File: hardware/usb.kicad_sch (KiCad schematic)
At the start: 4 parts, among them J201 USB_C_Receptacle_USB2.0, U201 SRV05-4

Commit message: update to kicad 9
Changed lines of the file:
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@@
 (kicad_sch
-	(version 20231120)
+	(version 20250114)
 	(generator "eeschema")
-	(generator_version "8.0")
+	(generator_version "9.0")
 	(paper "A4")
 	(title_block
@@
 	(label "USB_5V"
 		(at 151.13 74.93 0)
-		(fields_autoplaced yes)
 		(effects
 			(font
@@
 		(shape bidirectional)
 		(at 199.39 88.9 0)
-		(fields_autoplaced yes)
 		(effects
 			(font
@@
 		(shape bidirectional)
 		(at 135.89 86.36 0)
-		(fields_autoplaced yes)
 		(effects
 			(font
@@
 		(shape bidirectional)
 		(at 135.89 82.55 0)
-		(fields_autoplaced yes)
 		(effects
 			(font
@@
 		(shape bidirectional)
 		(at 135.89 96.52 0)
-		(fields_autoplaced yes)
 		(effects
 			(font
@@
 		(shape bidirectional)
 		(at 199.39 93.98 0)
-		(fields_autoplaced yes)
 		(effects
 			(font
@@
 		(shape bidirectional)
 		(at 135.89 80.01 0)
-		(fields_autoplaced yes)
-		(effects
-			(font
+		(effects
+			(font

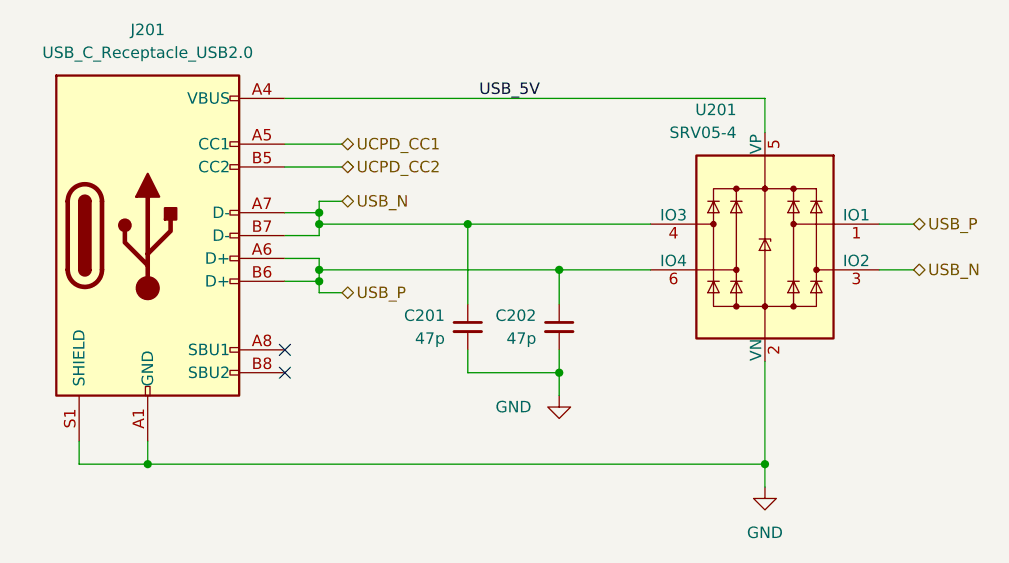
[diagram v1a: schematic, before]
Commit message: fix BOM to use basic parts again
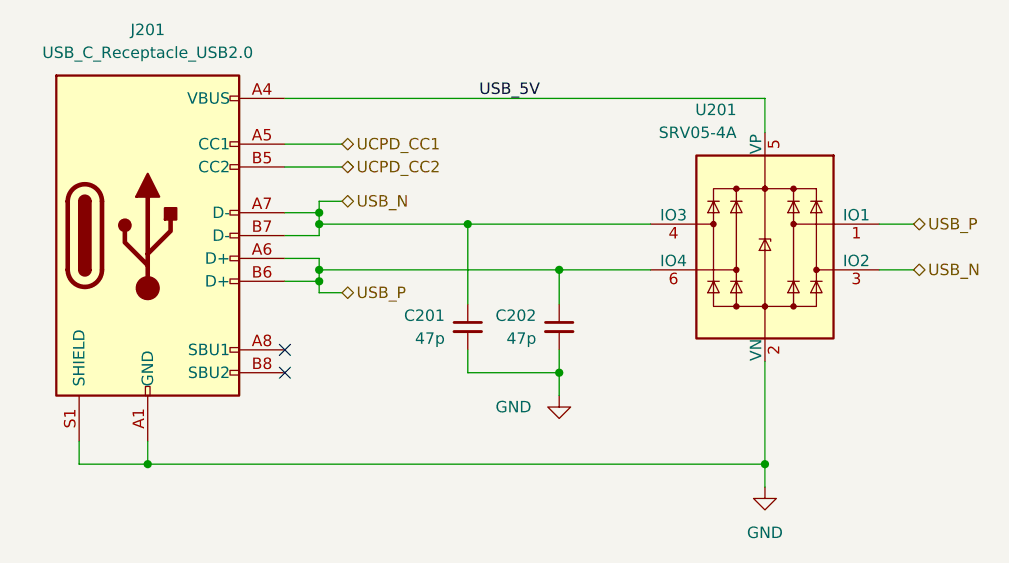
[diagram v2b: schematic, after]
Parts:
- U201: value SRV05-4 -> SRV05-4A; LCSC ID C7420376 -> C20615829
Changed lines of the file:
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@@
 			)
 		)
-		(property "Value" "SRV05-4"
+		(property "Value" "SRV05-4A"
 			(at 179.7303 78.74 0)
 			(effects
@@
 			)
 		)
-		(property "LCSC ID" "C7420376"
+		(property "LCSC ID" "C20615829"
 			(at 182.88 91.44 0)
 			(effects

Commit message: clean erc drc, pack sym, footprints into standalone lib
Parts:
- C201, C202: footprint Capacitor_SMD:C_0402_1005Metric -> lemon-pepper-footprints:C_0402_1005Metric; symbol Device:C_Small -> lemon-pepper-symbols:C_Small
- J201: footprint mechanical:usb_c -> lemon-pepper-footprints:usb_c; symbol Connector:USB_C_Receptacle_USB2.0 -> lemon-pepper-symbols:USB_C_Receptacle_USB2.0
- U201: footprint Package_TO_SOT_SMD:SOT-23-6 -> lemon-pepper-footprints:SOT-23-6; symbol Power_Protection:SRV05-4 -> lemon-pepper-symbols:SRV05-4
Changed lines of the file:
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@@
 	)
 	(symbol
-		(lib_id "Power_Protection:SRV05-4")
+		(lib_id "lemon-pepper-symbols:SRV05-4")
 		(at 182.88 91.44 0)
 		(mirror y)
@@
 			)
 		)
-		(property "Footprint" "Package_TO_SOT_SMD:SOT-23-6"
+		(property "Footprint" "lemon-pepper-footprints:SOT-23-6"
 			(at 165.1 102.87 0)
 			(effects
@@
 			)
 		)
-		(property "Description" ""
+		(property "Description" "ESD Protection Diodes with Low Clamping Voltage, SOT-23-6"
 			(at 182.88 91.44 0)
 			(effects
@@
 	)
 	(symbol
-		(lib_id "Connector:USB_C_Receptacle_USB2.0")
+		(lib_id "lemon-pepper-symbols:USB_C_Receptacle_USB2.0")
 		(at 114.3 90.17 0)
 		(unit 1)
@@
 			)
 		)
-		(property "Footprint" "mechanical:usb_c"
+		(property "Footprint" "lemon-pepper-footprints:usb_c"
 			(at 118.11 90.17 0)
 			(effects
@@
 	)
 	(symbol
-		(lib_id "Device:C_Small")
+		(lib_id "lemon-pepper-symbols:C_Small")
 		(at 160.02 100.33 0)
 		(unit 1)
@@
 			)
 		)
-		(property "Footprint" "Capacitor_SMD:C_0402_1005Metric"
+		(property "Footprint" "lemon-pepper-footprints:C_0402_1005Metric"
 			(at 160.02 100.33 0)
 			(effects
@@
 			)
 		)
-		(property "Description" ""
+		(property "Description" "Unpolarized capacitor, small symbol"
 			(at 160.02 100.33 0)
 			(effects
@@
 			)
 		)
-		(property "Description" ""
+		(property "Description" "Power symbol creates a global label with name \"GND\" , ground"
 			(at 160.02 107.95 0)
 			(effects
@@
 	)
 	(symbol
-		(lib_id "Device:C_Small")
+		(lib_id "lemon-pepper-symbols:C_Small")
 		(at 149.86 100.33 0)
 		(unit 1)
@@
 			)
 		)
-		(property "Footprint" "Capacitor_SMD:C_0402_1005Metric"
+		(property "Footprint" "lemon-pepper-footprints:C_0402_1005Metric"
 			(at 149.86 100.33 0)
 			(effects
@@
 			)
 		)
-		(property "Description" ""
+		(property "Description" "Unpolarized capacitor, small symbol"
 			(at 149.86 100.33 0)
 			(effects
@@
 			)
 		)
-		(property "Description" ""
+		(property "Description" "Power symbol creates a global label with name \"GND\" , ground"
 			(at 182.88 118.11 0)
 			(effects
